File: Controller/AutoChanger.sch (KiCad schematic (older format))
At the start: 44 parts, among them IC1 ATMEGA328P-A, P1 CONNECT, P2 USB_B, P3 1, P4 2, P5 3, P6 4, P7 ICSP, SW1 RESET, SW2 1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

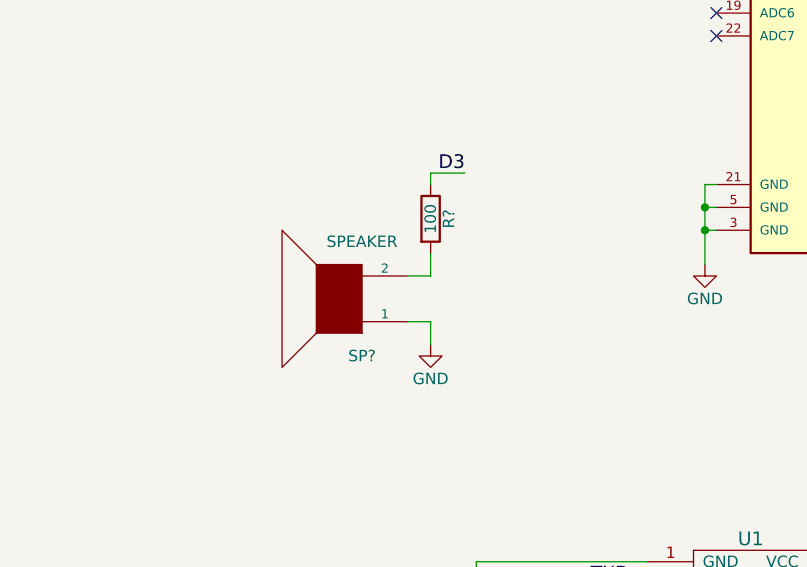
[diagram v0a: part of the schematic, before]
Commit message: Adding schematic pdfs and license
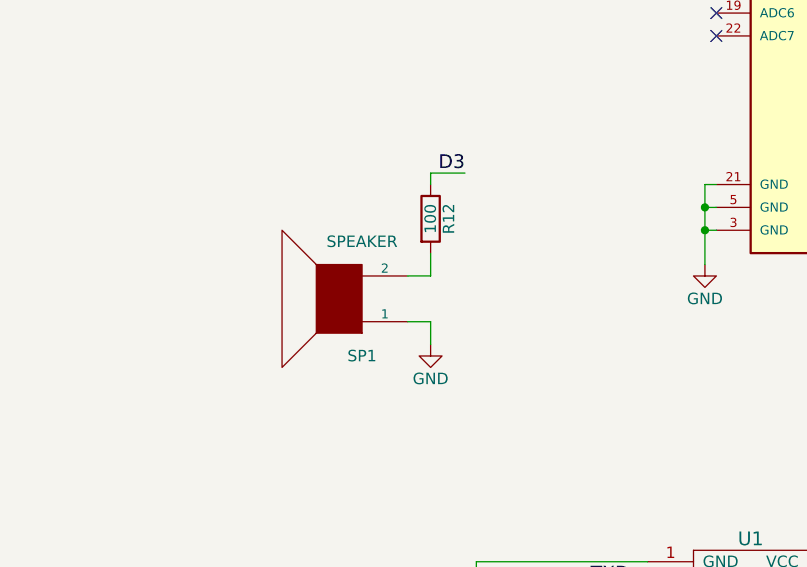
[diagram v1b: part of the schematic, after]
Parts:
- SP1: renamed from SP?; footprint (none) -> Buzzers_Beepers:Buzzer_12x9.5RM7.6
- gave numbers to parts that had none: 1
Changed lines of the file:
@@
 	8200 5750 8600 5750
 $Comp
-L SPEAKER SP?
+L SPEAKER SP1
 U 1 1 591DB397
 P 2100 4050
-F 0 "SP?" H 2000 4300 50  0000 C CNN
+F 0 "SP1" H 2000 4300 50  0000 C CNN
 F 1 "SPEAKER" H 2000 3800 50  0000 C CNN
-F 2 "" H 2100 4050 50  0000 C CNN
+F 2 "Buzzers_Beepers:Buzzer_12x9.5RM7.6" H 2100 4050 50  0001 C CNN
 F 3 "" H 2100 4050 50  0000 C CNN
 	1    2100 4050
@@
 $EndComp
 $Comp
-L GND #PWR?
+L GND #PWR047
 U 1 1 591DB68C
 P 2500 4250
-F 0 "#PWR?" H 2500 4000 50  0001 C CNN
+F 0 "#PWR047" H 2500 4000 50  0001 C CNN
 F 1 "GND" H 2500 4100 50  0000 C CNN
 F 2 "" H 2500 4250 50  0000 C CNN
@@
 $EndComp
 $Comp
-L R R?
+L R R12
 U 1 1 591DB76E
 P 2500 3700
-F 0 "R?" V 2580 3700 50  0000 C CNN
+F 0 "R12" V 2580 3700 50  0000 C CNN
 F 1 "100" V 2500 3700 50  0000 C CNN
 F 2 "Resistors_SMD:R_0603_HandSoldering" V 2430 3700 50  0001 C CNN

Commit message: Updated board design.
Heaps more caps.  Thanks @projectgus
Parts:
- added C10, C11, C12, C13: 1uF, Capacitors_SMD:C_0603_HandSoldering, symbol C
- added C9: 100nF, Capacitors_SMD:C_0603_HandSoldering, symbol C
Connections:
- wire segments 169 -> 178
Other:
- moved on the sheet: C1, C2, C3, P3, P4, P5, P6

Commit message: Updated design
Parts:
- removed C1: 1uF, Capacitors_SMD:C_0603_HandSoldering, symbol C
- removed X1: 16Mhz, Crystals:Crystal_SMD_3225-4pin_3.2x2.5mm_HandSoldering, symbol CRYSTAL_4PIN_SMD
- added P10, P11: SENSOR, Pin_Headers:Pin_Header_Straight_1x03_Pitch2.54mm, symbol CONN_01X03
- added P8, P9: M3, Connect:1pin, symbol CONN_01X01
- added Q1: 2n7002, TO_SOT_Packages_SMD:SOT-23_Handsoldering, symbol Q_PNP_BEC
- added R13: 1M, Resistors_SMD:R_0603_HandSoldering, symbol R
- added Y2: 16Mhz, Crystals:Crystal_HC49-U_Vertical, symbol Crystal
- C2, C3: value 15pF -> 22pF
- U3: footprint Pin_Headers:Pin_Header_Angled_2x02_Pitch2.54mm -> libs:ITR9606
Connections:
- net labels added: PWR_DOWN
- wire segments 178 -> 194
- no-connect marks 10 -> 12
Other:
- moved on the sheet: C2, C3, R12, R4, R5, SP1, U3

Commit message: Updated circuit board
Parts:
- removed Q1: 2n7002, TO_SOT_Packages_SMD:SOT-23_Handsoldering, symbol Q_PNP_BEC
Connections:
- net labels removed: PWR_DOWN
- wire segments 194 -> 185
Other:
- moved on the sheet: D1, P2
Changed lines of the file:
@@
 EESchema Schematic File Version 2
+LIBS:AutoChanger-rescue
 LIBS:power
 LIBS:device
@@
 L USB_B P2
 U 1 1 59171051
-P 1000 1150
-F 0 "P2" H 1200 950 50  0000 C CNN
-F 1 "USB_B" H 950 1350 50  0000 C CNN
-F 2 "Connect:USB_B" V 950 1050 50  0001 C CNN
-F 3 "" V 950 1050 50  0000 C CNN
-	1    1000 1150
-	0    -1   1    0
+P 900 950
+F 0 "P2" H 1100 750 50  0000 C CNN
+F 1 "USB_B" H 850 1150 50  0000 C CNN
+F 2 "Connect:USB_B" V 850 850 50  0001 C CNN
+F 3 "" V 850 850 50  0000 C CNN
+	1    900  950
+	1    0    0    -1
 $EndComp
 $Comp
 L GND #PWR01
 U 1 1 591711CC
-P 900 1550
-F 0 "#PWR01" H 900 1300 50  0001 C CNN
-F 1 "GND" H 900 1400 50  0000 C CNN
-F 2 "" H 900 1550 50  0000 C CNN
-F 3 "" H 900 1550 50  0000 C CNN
-	1    900  1550
-	1    0    0    -1
-$EndComp
-Wire Wire Line
-	1300 1250 1350 1250
-Wire Wire Line
-	1350 1250 1350 1500
-Wire Wire Line
-	1350 1500 900  1500
-Wire Wire Line
-	900  1450 900  1550
-Connection ~ 900  1500
+P 800 1450
+F 0 "#PWR01" H 800 1200 50  0001 C CNN
+F 1 "GND" H 800 1300 50  0000 C CNN
+F 2 "" H 800 1450 50  0000 C CNN
+F 3 "" H 800 1450 50  0000 C CNN
+	1    800  1450
+	1    0    0    -1
+$EndComp
 $Comp
 L +5V #PWR02
 U 1 1 59171318
-P 2000 900
-F 0 "#PWR02" H 2000 750 50  0001 C CNN
-F 1 "+5V" H 2000 1040 50  0000 C CNN
-F 2 "" H 2000 900 50  0000 C CNN
-F 3 "" H 2000 900 50  0000 C CNN
-	1    2000 900
-	1    0    0    -1
-$EndComp
-Wire Wire Line
-	1300 950  1600 950
-Wire Wire Line
-	1300 1050 1550 1050
-Wire Wire Line
-	1300 1150 1550 1150
-Text Label 1550 1050 2    60   ~ 0
+P 1800 700
+F 0 "#PWR02" H 1800 550 50  0001 C CNN
+F 1 "+5V" H 1800 840 50  0000 C CNN
+F 2 "" H 1800 700 50  0000 C CNN
+F 3 "" H 1800 700 50  0000 C CNN
+	1    1800 700
+	1    0    0    -1
+$EndComp
+Wire Wire Line
+	1200 750  1400 750
+Wire Wire Line
+	1200 950  1350 950
+Wire Wire Line
+	1200 1050 1350 1050
+Text Label 1350 1050 2    60   ~ 0
 D-
-Text Label 1550 1150 2    60   ~ 0
+Text Label 1350 950  2    60   ~ 0
 D+
 $Comp
@@
 	6150 5150 6150 5050
 Wire Wire Line
-	6150 5450 6150 5550
-Wire Wire Line
-	6150 5950 6150 6050
+	6150 5450 6150 5600
+Wire Wire Line
+	6150 5900 6150 6050
 Wire Wire Line
 	6150 6050 6400 6050
@@
 	5700 5150 5700 5050
 Wire Wire Line
-	5700 5450 5700 5550
-Wire Wire Line
-	5700 5950 5700 6050
+	5700 5450 5700 5600
+Wire Wire Line
+	5700 5900 5700 6050
 Wire Wire Line
 	5700 6050 5950 6050
@@
 	6600 5150 6600 5050
 Wire Wire Line
-	6600 5550 6600 5450
+	6600 5600 6600 5450
 $Comp
 L GND #PWR033
@@
 $EndComp
 Wire Wire Line
-	6600 6050 6600 5950
+	6600 6050 6600 5900
 $Comp
 L D D1
 U 1 1 59183DA3
-P 1750 950
-F 0 "D1" H 1750 1050 50  0000 C CNN
-F 1 "D" H 1750 850 50  0000 C CNN
-F 2 "Diodes_SMD:D_SMA_Handsoldering" H 1750 950 50  0001 C CNN
-F 3 "" H 1750 950 50  0000 C CNN
-	1    1750 950
+P 1550 750
+F 0 "D1" H 1550 850 50  0000 C CNN
+F 1 "D" H 1550 650 50  0000 C CNN
+F 2 "Diodes_SMD:D_SMA_Handsoldering" H 1550 750 50  0001 C CNN
+F 3 "" H 1550 750 50  0000 C CNN
+	1    1550 750
 	-1   0    0    1
 $EndComp
 Wire Wire Line
-	1900 950  2000 950
-Wire Wire Line
-	2000 950  2000 900
+	1700 750  1800 750
+Wire Wire Line
+	1800 750  1800 700
 $Comp
 L CONN_01X03 P4
@@
 Text Label 6000 3250 2    60   ~ 0
 D2
-Text Label 6350 1950 2    60   ~ 0
+Text Label 6350 1950 2    60   Italic 0
 D13
 Text Label 6350 1850 2    60   Italic 0
@@
 Connection ~ 1900 7200
 $Comp
-L Q_PNP_BEC Q1
-U 1 1 599890D0
-P 7650 3450
-F 0 "Q1" H 7950 3500 50  0000 R CNN
-F 1 "2n7002" H 8250 3400 50  0000 R CNN
-F 2 "TO_SOT_Packages_SMD:SOT-23_Handsoldering" H 7850 3550 50  0001 C CNN
-F 3 "" H 7650 3450 50  0000 C CNN
-	1    7650 3450
-	1    0    0    -1
-$EndComp
-Text Label 7200 3450 0    60   ~ 0
-D13
-Wire Wire Line
-	7450 3450 7200 3450
-Wire Wire Line
-	7750 3650 7750 3750
-$Comp
 L +5V #PWR043
 U 1 1 5998A933
-P 7750 3150
-F 0 "#PWR043" H 7750 3000 50  0001 C CNN
-F 1 "+5V" H 7750 3290 50  0000 C CNN
-F 2 "" H 7750 3150 50  0000 C CNN
-F 3 "" H 7750 3150 50  0000 C CNN
-	1    7750 3150
-	1    0    0    -1
-$EndComp
-Wire Wire Line
-	7750 3250 7750 3150
-Text Label 8300 3750 2    60   ~ 0
-PWR_DOWN
-Wire Wire Line
-	7750 3750 8300 3750
-Text Label 7950 1600 2    60   ~ 0
-PWR_DOWN
-Text Label 7950 700  2    60   ~ 0
-PWR_DOWN
-Text Label 8900 700  2    60   ~ 0
-PWR_DOWN
-Text Label 8900 1600 2    60   ~ 0
-PWR_DOWN
-Wire Wire Line
-	8900 700  8400 700
-Wire Wire Line
-	7450 700  7950 700
-Wire Wire Line
-	7450 1600 7950 1600
-Wire Wire Line
-	8400 1600 8900 1600
+P 7450 700
+F 0 "#PWR043" H 7450 550 50  0001 C CNN
+F 1 "+5V" H 7450 840 50  0000 C CNN
+F 2 "" H 7450 700 50  0000 C CNN
+F 3 "" H 7450 700 50  0000 C CNN
+	1    7450 700
+	1    0    0    -1
+$EndComp
 $Comp
 L CONN_01X01 P8
@@
 Wire Wire Line
 	2800 3550 2650 3550
+$Comp
+L +5V #PWR048
+U 1 1 59B6A4B4
+P 8400 700
+F 0 "#PWR048" H 8400 550 50  0001 C CNN
+F 1 "+5V" H 8400 840 50  0000 C CNN
+F 2 "" H 8400 700 50  0000 C CNN
+F 3 "" H 8400 700 50  0000 C CNN
+	1    8400 700
+	1    0    0    -1
+$EndComp
+$Comp
+L +5V #PWR049
+U 1 1 59B6A55E
+P 8400 1600
+F 0 "#PWR049" H 8400 1450 50  0001 C CNN
+F 1 "+5V" H 8400 1740 50  0000 C CNN
+F 2 "" H 8400 1600 50  0000 C CNN
+F 3 "" H 8400 1600 50  0000 C CNN
+	1    8400 1600
+	1    0    0    -1
+$EndComp
+$Comp
+L +5V #PWR050
+U 1 1 59B6A608
+P 7450 1600
+F 0 "#PWR050" H 7450 1450 50  0001 C CNN
+F 1 "+5V" H 7450 1740 50  0000 C CNN
+F 2 "" H 7450 1600 50  0000 C CNN
+F 3 "" H 7450 1600 50  0000 C CNN
+	1    7450 1600
+	1    0    0    -1
+$EndComp
+Wire Wire Line
+	800  1350 800  1450
+Wire Wire Line
+	800  1400 900  1400
+Wire Wire Line
+	900  1400 900  1350
+Connection ~ 800  1400
 $EndSCHEMATC

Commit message: Updated version
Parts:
- added P12: LOGO, libs:logo, symbol CONN_01X01
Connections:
- net D11: now also P7.4 (P4); no longer P7.1 (P1)
- net D12: now also P7.1 (P1); no longer P7.4 (P4)
- no-connect marks 12 -> 13
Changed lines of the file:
@@
 Wire Wire Line
 	9750 5750 9450 5750
+Text Label 6000 1850 2    60   ~ 0
+MISO
 Text Label 6000 1750 2    60   ~ 0
-MISO
-Text Label 6000 1850 2    60   ~ 0
 MOSI
 Text Label 6000 1950 2    60   ~ 0
@@
 	900  1400 900  1350
 Connection ~ 800  1400
+$Comp
+L CONN_01X01 P12
+U 1 1 59CBCEE5
+P 3050 1200
+F 0 "P12" H 3050 1300 50  0000 C CNN
+F 1 "LOGO" V 3150 1200 50  0000 C CNN
+F 2 "libs:logo" H 3050 1200 50  0001 C CNN
+F 3 "" H 3050 1200 50  0000 C CNN
+	1    3050 1200
+	1    0    0    -1
+$EndComp
+NoConn ~ 2850 1200
 $EndSCHEMATC

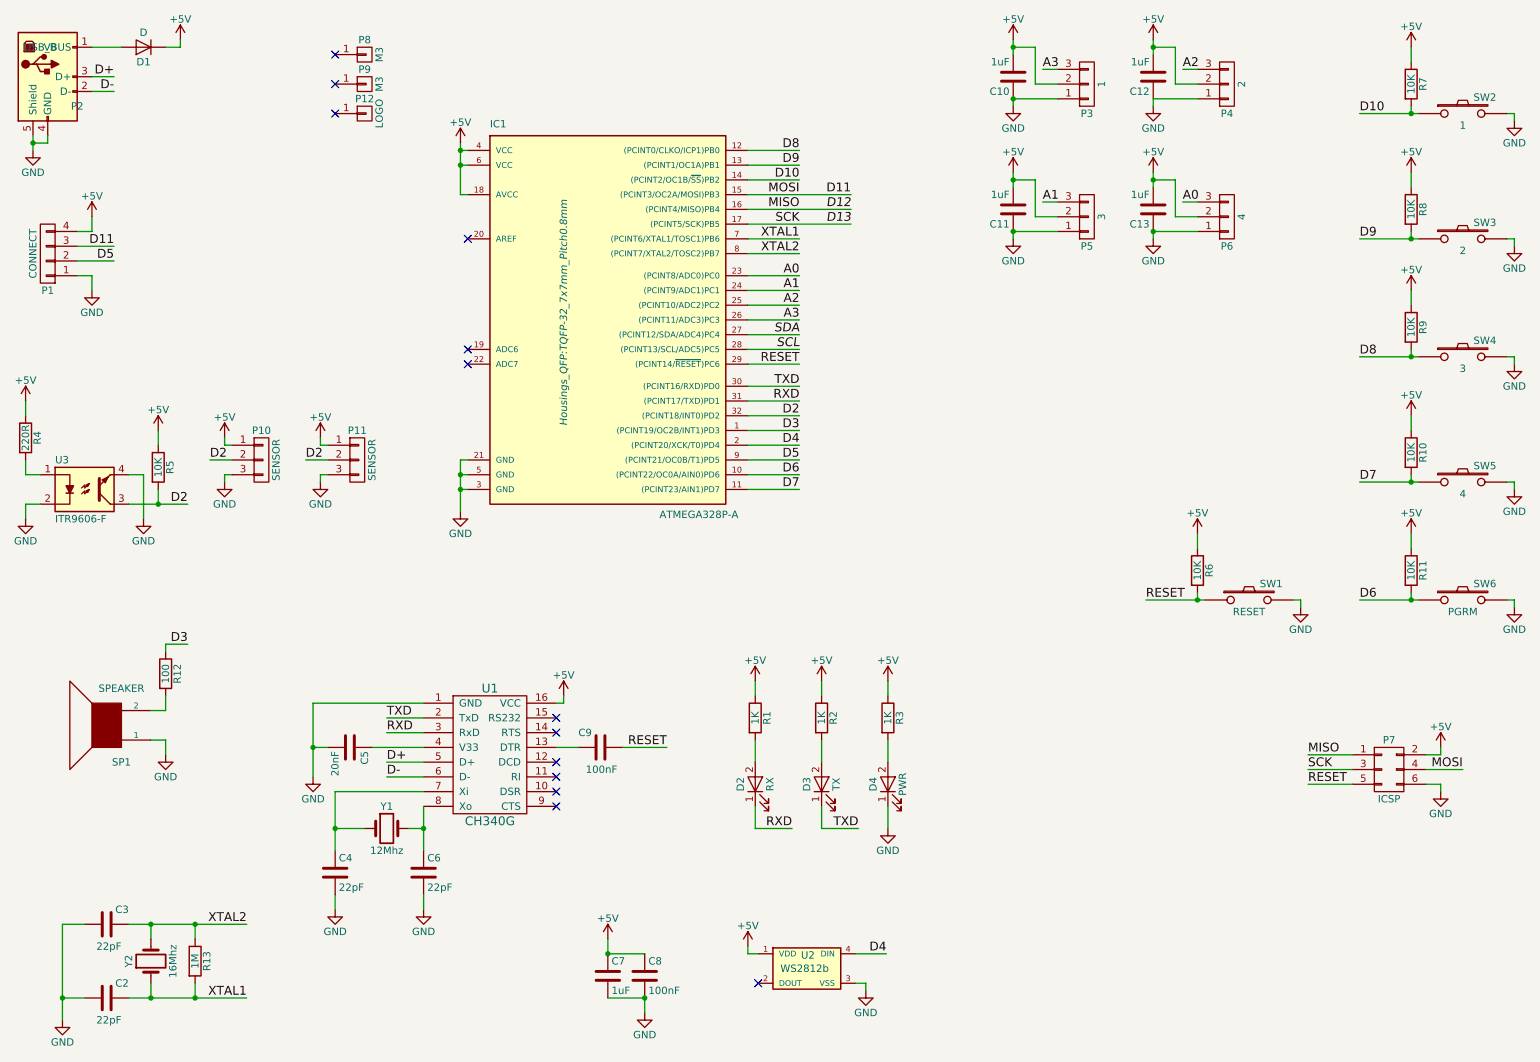
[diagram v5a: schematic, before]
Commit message: New Nano version
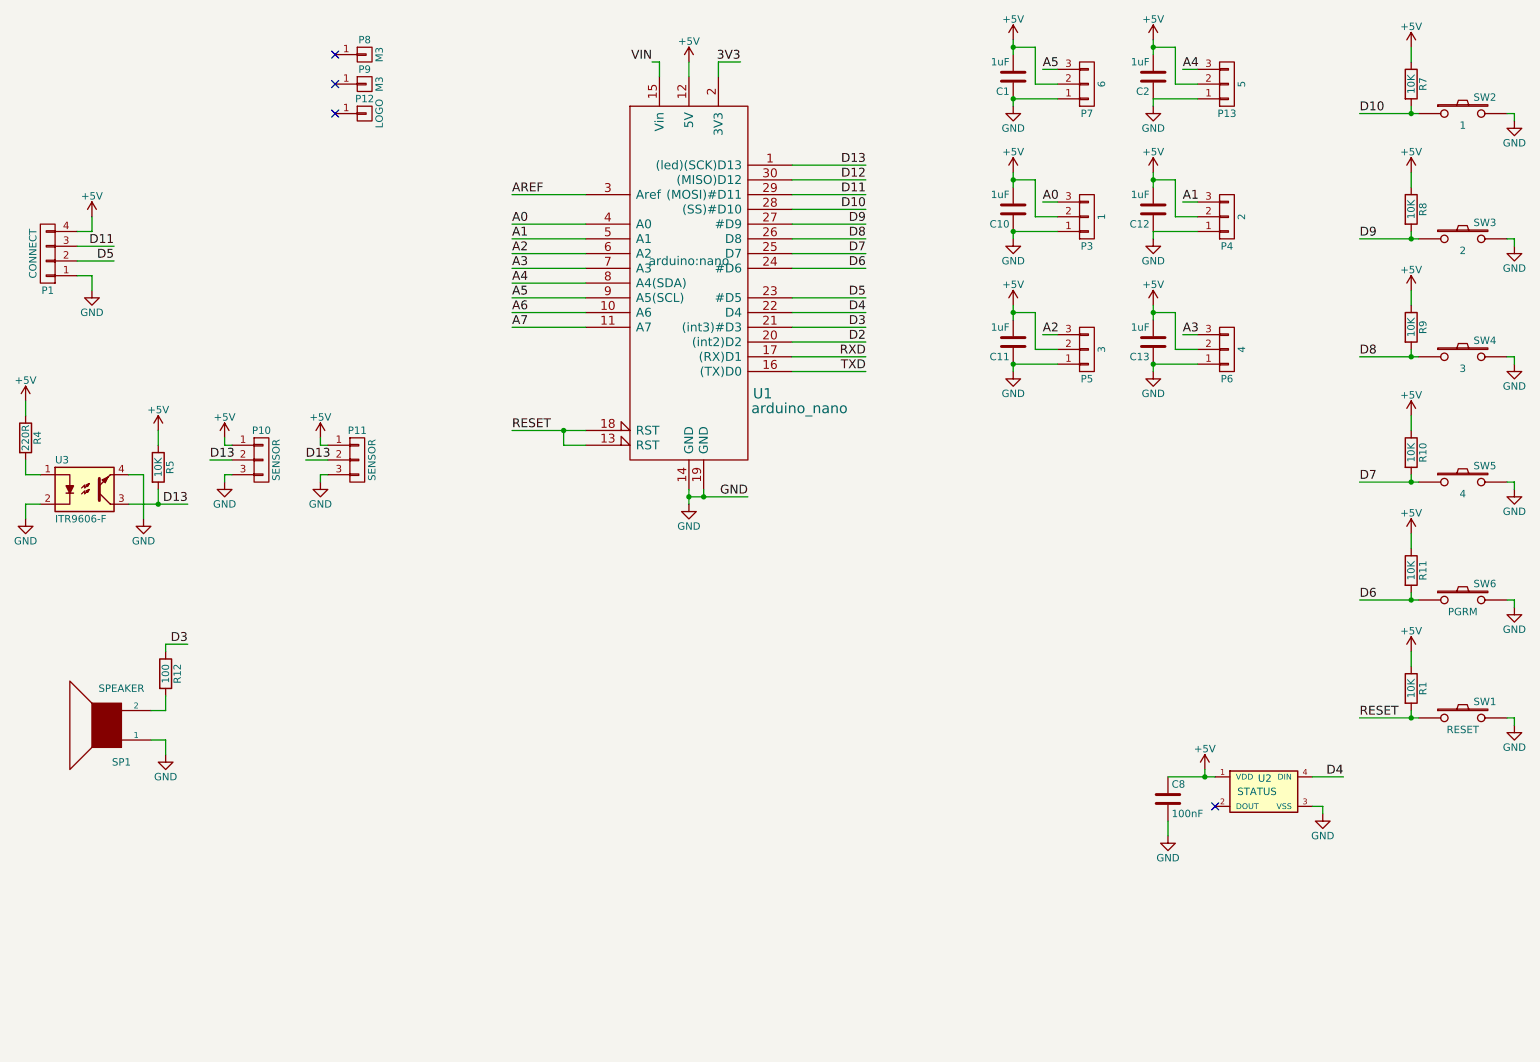
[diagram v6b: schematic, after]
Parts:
- removed C3, C4, C6: 22pF, Capacitors_SMD:C_0603_HandSoldering, symbol C
- removed C5: 20nF, Capacitors_SMD:C_0603_HandSoldering, symbol C
- removed C7: 1uF, Capacitors_SMD:C_0603_HandSoldering, symbol C
- removed C9: 100nF, Capacitors_SMD:C_0603_HandSoldering, symbol C
- removed D1: D, Diodes_SMD:D_SMA_Handsoldering, symbol D
- removed D2: RX, LEDs:LED_0603, symbol LED
- removed D3: TX, LEDs:LED_0603, symbol LED
- removed D4: PWR, LEDs:LED_0603, symbol LED
- removed IC1: ATMEGA328P-A, Housings_QFP:TQFP-32_7x7mm_Pitch0.8mm, symbol ATMEGA328P-A
- removed P2: USB_B, Connect:USB_B, symbol USB_B
- removed P7: ICSP, Pin_Headers:Pin_Header_Straight_2x03_Pitch2.54mm, symbol CONN_02X03
- removed R13: 1M, Resistors_SMD:R_0603_HandSoldering, symbol R
- removed R2, R3: 1K, Resistors_SMD:R_0603_HandSoldering, symbol R
- removed R6: 10K, Resistors_SMD:R_0603_HandSoldering, symbol R
- removed U1: CH340G, SMD_Packages:SO-16-N, symbol CH340G
- removed Y1: 12Mhz, Crystals:Crystal_HC49-U_Vertical, symbol Crystal
- removed Y2: 16Mhz, Crystals:Crystal_HC49-U_Vertical, symbol Crystal
- added C1: 1uF, Capacitors_SMD:C_0603_HandSoldering, symbol C
- added P13: 5, Pin_Headers:Pin_Header_Straight_1x03_Pitch2.54mm, symbol CONN_01X03
- added P7: 6, Pin_Headers:Pin_Header_Straight_1x03_Pitch2.54mm, symbol CONN_01X03
- added U1: arduino_nano, arduino:nano, symbol arduino_nano
- C2: value 22pF -> 1uF
- P1: footprint Pin_Headers:Pin_Header_Angled_2x02_Pitch2.54mm -> Pin_Headers:Pin_Header_Straight_2x02_Pitch2.54mm
- R1: value 1K -> 10K
- U2: value WS2812b -> STATUS
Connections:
- net XTAL1 is gone; now on net +5V: C2.2
- net +5V: now also C1.2, P13.2 (P2), P7.2 (P2), U1.12 (5V)
- net A0: now also P3.3 (P3), U1.4 (A0); no longer P6.3 (P3)
- net A1: now also P4.3 (P3), U1.5 (A1); no longer P5.3 (P3)
- net A2: now also P5.3 (P3), U1.6 (A2); no longer P4.3 (P3)
- net A3: now also P6.3 (P3), U1.7 (A3); no longer P3.3 (P3)
- net D10: now also U1.28 ((SS)#D10)
- net D11: now also U1.29 ((MOSI)#D11)
- net D12: now also U1.30 ((MISO)D12)
- net D13: now also P10.2 (P2), P11.2 (P2), R5.2, U3.3, U1.1 ((led)(SCK)D13)
- net D2: now also U1.20 ((int2)D2); no longer P10.2 (P2), P11.2 (P2), R5.2, U3.3
- net D3: now also U1.21 ((int3)#D3)
- net D4: now also U1.22 (D4)
- net D5: now also U1.23 (#D5)
- net D6: now also U1.24 (#D6)
- net D7: now also U1.25 (D7)
- net D8: now also U1.26 (D8)
- net D9: now also U1.27 (#D9)
- net GND: now also C1.1, P13.1 (P1), P7.1 (P1), U1.14 (GND), U1.19 (GND)
- net RESET: now also R1.2, U1.13 (RST), U1.18 (RST)
- net RXD: now also U1.17 ((RX)D1)
- net TXD: now also U1.16 ((TX)D0)
- new net 3V3: U1.2 (3V3)
- new net A4: P13.3 (P3), U1.8 (A4(SDA))
- new net A5: P7.3 (P3), U1.9 (A5(SCL))
- new net A6: U1.10 (A6)
- new net A7: U1.11 (A7)
- new net AREF: U1.3 (Aref)
- new net VIN: U1.15 (Vin)
- no-connect marks 13 -> 4
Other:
- moved on the sheet: C10, C11, C12, C13, C8, P3, P4, P5, P6, U2

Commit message: Updated designs across the board
So, lots of small changes as I've tweaked the design.

In order to improve manufacturing, I've changed to 3d printing the main body.
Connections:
- net +5V: now also U3.3; no longer R5.1
- net D13: now also R5.1, U3.4; no longer R5.2, U3.3
- net GND: now also R5.2; no longer U3.4
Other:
- moved on the sheet: R5
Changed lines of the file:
@@
 L +5V #PWR05
 U 1 1 59174710
-P 1650 3350
-F 0 "#PWR05" H 1650 3200 50  0001 C CNN
-F 1 "+5V" H 1650 3490 50  0000 C CNN
-F 2 "" H 1650 3350 50  0000 C CNN
-F 3 "" H 1650 3350 50  0000 C CNN
-	1    1650 3350
+P 1500 3500
+F 0 "#PWR05" H 1500 3350 50  0001 C CNN
+F 1 "+5V" H 1500 3640 50  0000 C CNN
+F 2 "" H 1500 3500 50  0000 C CNN
+F 3 "" H 1500 3500 50  0000 C CNN
+	1    1500 3500
 	1    0    0    -1
 $EndComp
@@
 L R R5
 U 1 1 59174742
-P 1650 3600
-F 0 "R5" V 1730 3600 50  0000 C CNN
-F 1 "10K" V 1650 3600 50  0000 C CNN
-F 2 "Resistors_SMD:R_0603_HandSoldering" V 1580 3600 50  0001 C CNN
-F 3 "" H 1650 3600 50  0000 C CNN
-	1    1650 3600
+P 1600 4000
+F 0 "R5" V 1680 4000 50  0000 C CNN
+F 1 "10K" V 1600 4000 50  0000 C CNN
+F 2 "Resistors_SMD:R_0603_HandSoldering" V 1530 4000 50  0001 C CNN
+F 3 "" H 1600 4000 50  0000 C CNN
+	1    1600 4000
 	1    0    0    -1
 $EndComp
@@
 L GND #PWR06
 U 1 1 59174829
-P 1550 3950
-F 0 "#PWR06" H 1550 3700 50  0001 C CNN
-F 1 "GND" H 1550 3800 50  0000 C CNN
-F 2 "" H 1550 3950 50  0000 C CNN
-F 3 "" H 1550 3950 50  0000 C CNN
-	1    1550 3950
-	1    0    0    -1
-$EndComp
-Wire Wire Line
-	1450 3650 1550 3650
-Connection ~ 1650 3850
+P 1600 4250
+F 0 "#PWR06" H 1600 4000 50  0001 C CNN
+F 1 "GND" H 1600 4100 50  0000 C CNN
+F 2 "" H 1600 4250 50  0000 C CNN
+F 3 "" H 1600 4250 50  0000 C CNN
+	1    1600 4250
+	1    0    0    -1
+$EndComp
+Wire Wire Line
+	1450 3650 1800 3650
 $Comp
 L C C8
@@
 Text Label 9800 2050 0    60   ~ 0
 D9
-Text Label 1850 3850 2    60   ~ 0
+Text Label 1800 3650 2    60   ~ 0
 D13
 $Comp
@@
 	1100 2200 1350 2200
 Wire Wire Line
-	1650 3350 1650 3450
-Wire Wire Line
-	1650 3750 1650 3850
-Wire Wire Line
-	1550 3650 1550 3950
-Wire Wire Line
-	1450 3850 1850 3850
+	1600 3650 1600 3850
 $Comp
 L SPEAKER SP1
@@
 RXD
 Wire Wire Line
-	4550 3350 4050 3350
+	4050 3350 4550 3350
 Text Label 4050 3350 0    60   ~ 0
 RESET
@@
 Text Label 2650 3550 0    60   ~ 0
 D13
+Wire Wire Line
+	1450 3850 1500 3850
+Wire Wire Line
+	1500 3850 1500 3500
+Wire Wire Line
+	1600 4150 1600 4250
+Connection ~ 1600 3650
 $EndSCHEMATC
